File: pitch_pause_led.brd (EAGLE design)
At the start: 30.5 x 78.7 mm, 8 parts

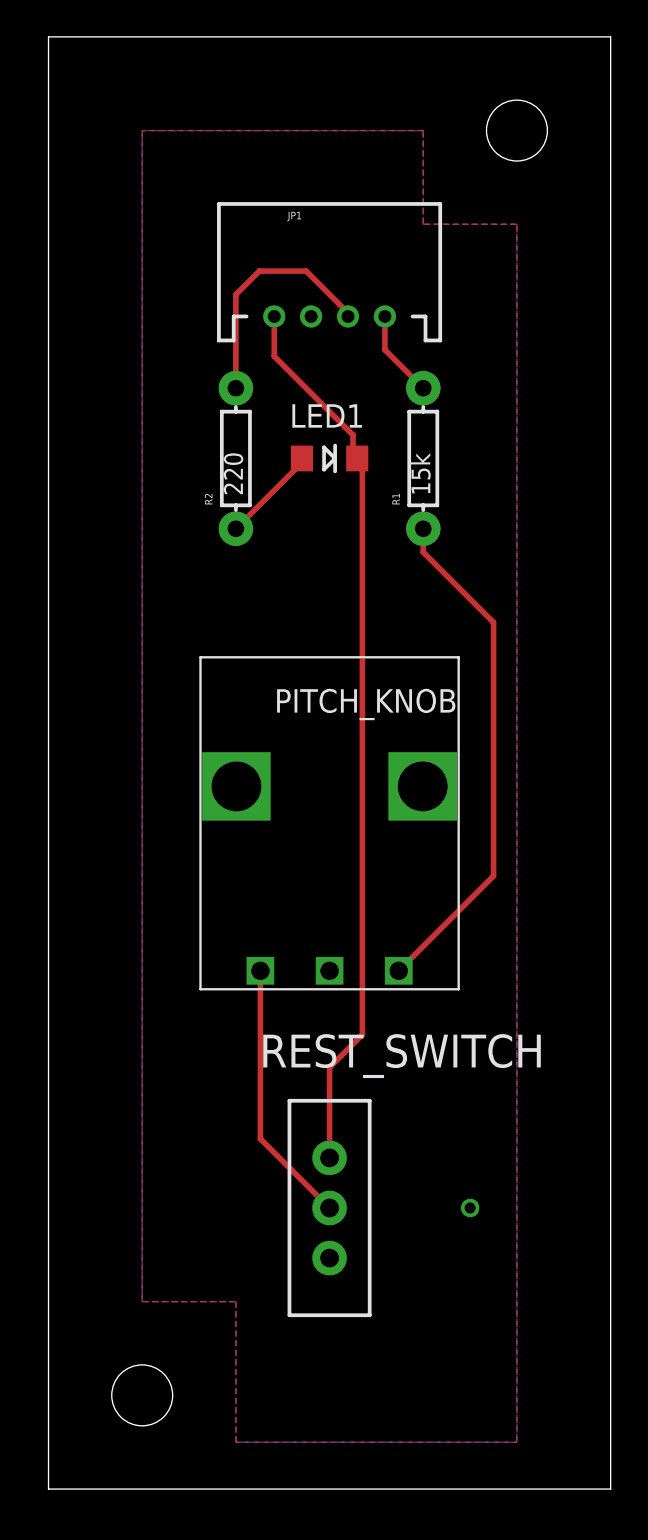
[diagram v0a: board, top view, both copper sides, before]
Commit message: through hole led on mini boards
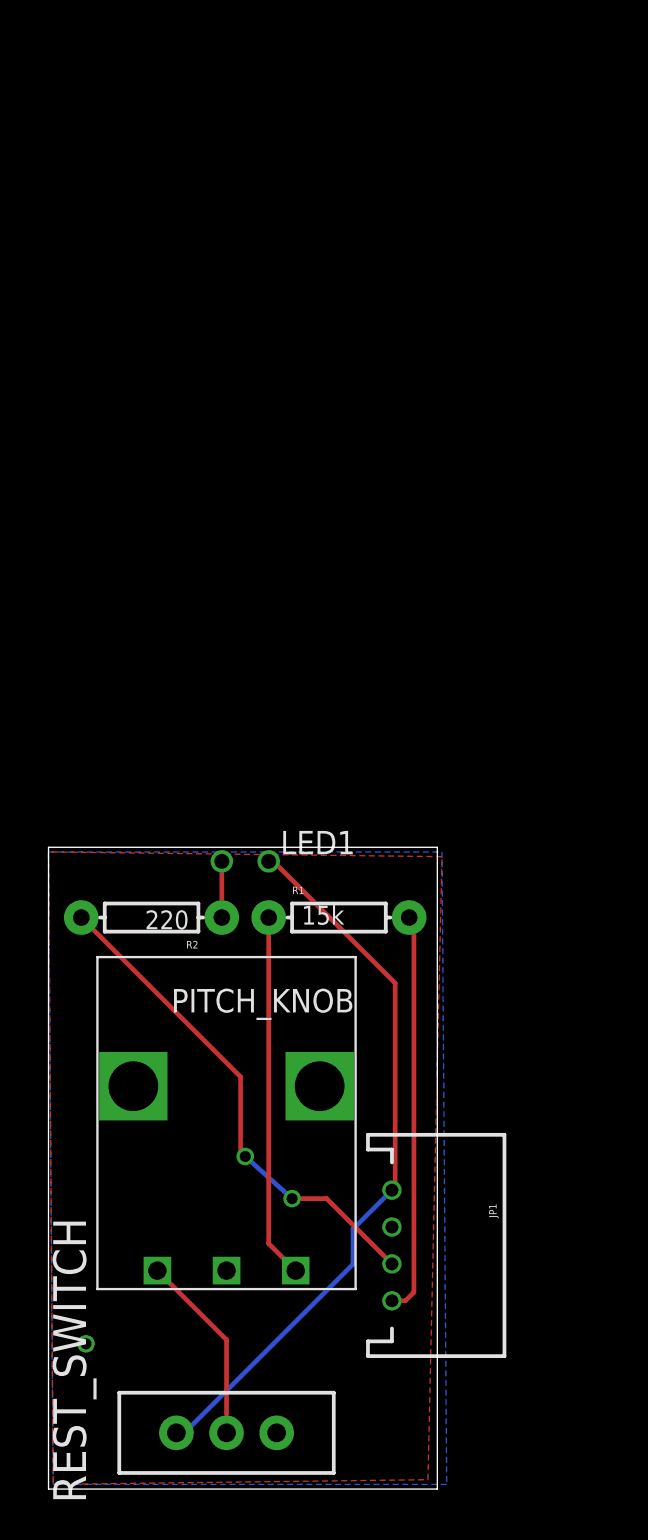
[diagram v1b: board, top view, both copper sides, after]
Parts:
- removed STANDOFF1, STANDOFF2: STAND-OFF, SparkFun-Electromechanical:STAND-OFF
- LED1: device LilyPad-Wearables:LED-1206 -> SparkFun-LED:LED3MM-NS
- moved JP1 56.0 mm to (23.6, 13.2), turned to 270 degrees
- moved R1 25.3 mm to (15.7, 31.0), turned to 0 degrees
- moved R2 25.3 mm to (5.59, 31.0), turned to 180 degrees
- moved LED1 22.3 mm to (10.7, 34.0)
- moved PITCH_KNOB 17.2 mm to (9.65, 21.8)
- moved REST_SWITCH 13.4 mm to (9.65, 3.05), turned to 90 degrees
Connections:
- net GND: now also LED1.K; no longer LED1.C
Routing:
- net VCC: track 4.75 -> 21.8 mm
- net LED: track 12.8 -> 27.1 mm, vias 0 -> 2
- net GND: track 48.3 -> 39.1 mm
- net N$2: track 27.7 -> 19.8 mm
- net N$1: track 14.4 -> 10.3 mm
- net N$4: track 5.29 -> 3.05 mm
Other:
- board size 30.5 x 78.7 mm -> 21.1 x 34.8 mm
